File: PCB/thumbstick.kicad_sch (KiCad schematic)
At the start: 2 parts

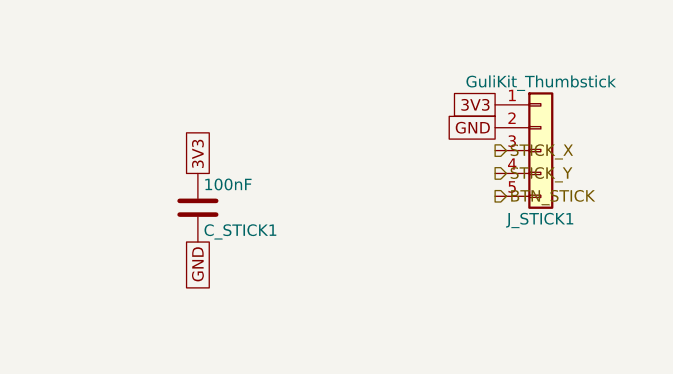
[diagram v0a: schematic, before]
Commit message: refactor: updated gulikit footprint
This updates the gulikit thumbstick footprint to be accurate.
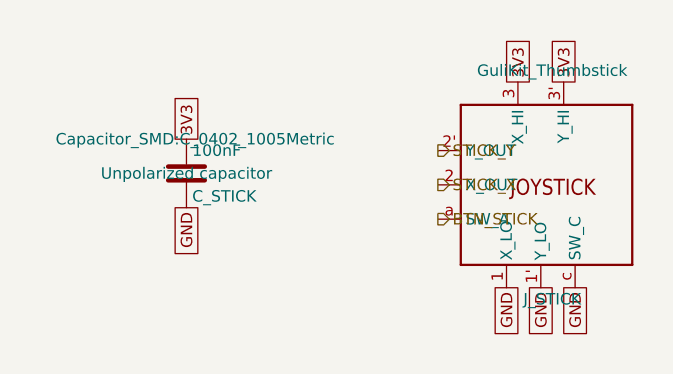
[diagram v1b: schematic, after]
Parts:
- removed C_STICK1: 100nF, Capacitor_SMD:C_0402_1005Metric, symbol Device:C
- removed J_STICK1: GuliKit_Thumbstick, Connector_PinHeader_2.54mm:PinHeader_1x05_P2.54mm_Vertical, symbol Connector_Generic:Conn_01x05
- added C_STICK: 100nF, Capacitor_SMD:C_0402_1005Metric, symbol Device:C
- added J_STICK: GuliKit_Thumbstick, SnipsControllers_Custom:GuliKit_HallStick, symbol SnipsControllers_Custom:GuliKit_HallStick
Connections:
- net 3V3: now also C_STICK.1, J_STICK.3 (X_HI), J_STICK.3' (Y_HI)
- net BTN_STICK: now also J_STICK.a (SW_A)
- net GND: now also C_STICK.2, J_STICK.1 (X_LO), J_STICK.1' (Y_LO), J_STICK.c (SW_C)
- net STICK_X: now also J_STICK.2 (X_OUT)
- net STICK_Y: now also J_STICK.2' (Y_OUT)
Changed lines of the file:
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@@
 	(global_label "GND"
 		(shape passive)
-		(at 129.54 111.76 270)
+		(at 163.83 116.84 270)
 		(fields_autoplaced yes)
 		(effects
@@
 		)
 		(property "Intersheetrefs" "${INTERSHEET_REFS}"
-			(at 129.54 111.76 0)
+			(at 163.83 116.84 0)
+			(hide yes)
+			(show_name no)
+			(do_not_autoplace no)
+			(effects
+				(font
+					(size 1.27 1.27)
+				)
+			)
+		)
+	)
+	(global_label "GND"
+		(shape passive)
+		(at 128.27 107.95 270)
+		(fields_autoplaced yes)
+		(effects
+			(font
+				(size 1.27 1.27)
+			)
+			(justify right)
+		)
+		(property "Intersheetrefs" "${INTERSHEET_REFS}"
+			(at 128.27 107.95 0)
 			(hide yes)
 			(show_name no)
@@
 	(global_label "3V3"
 		(shape passive)
-		(at 162.56 96.52 180)
+		(at 128.27 100.33 90)
+		(fields_autoplaced yes)
+		(effects
+			(font
+				(size 1.27 1.27)
+			)
+			(justify left)
+		)
+		(property "Intersheetrefs" "${INTERSHEET_REFS}"
+			(at 128.27 100.33 0)
+			(hide yes)
+			(show_name no)
+			(do_not_autoplace no)
+			(effects
+				(font
+					(size 1.27 1.27)
+				)
+			)
+		)
+	)
+	(global_label "3V3"
+		(shape passive)
+		(at 165.1 93.98 90)
+		(fields_autoplaced yes)
+		(effects
+			(font
+				(size 1.27 1.27)
+			)
+			(justify left)
+		)
+		(property "Intersheetrefs" "${INTERSHEET_REFS}"
+			(at 165.1 93.98 0)
+			(hide yes)
+			(show_name no)
+			(do_not_autoplace no)
+			(effects
+				(font
+					(size 1.27 1.27)
+				)
+			)
+		)
+	)
+	(global_label "3V3"
+		(shape passive)
+		(at 170.18 93.98 90)
+		(fields_autoplaced yes)
+		(effects
+			(font
+				(size 1.27 1.27)
+			)
+			(justify left)
+		)
+		(property "Intersheetrefs" "${INTERSHEET_REFS}"
+			(at 170.18 93.98 0)
+			(hide yes)
+			(show_name no)
+			(do_not_autoplace no)
+			(effects
+				(font
+					(size 1.27 1.27)
+				)
+			)
+		)
+	)
+	(global_label "GND"
+		(shape passive)
+		(at 171.45 116.84 270)
 		(fields_autoplaced yes)
 		(effects
@@
 		)
 		(property "Intersheetrefs" "${INTERSHEET_REFS}"
-			(at 162.56 96.52 0)
-			(hide yes)
-			(show_name no)
-			(do_not_autoplace no)
-			(effects
-				(font
-					(size 1.27 1.27)
-				)
-			)
-		)
-	)
-	(global_label "3V3"
-		(shape passive)
-		(at 129.54 104.14 90)
-		(fields_autoplaced yes)
-		(effects
-			(font
-				(size 1.27 1.27)
-			)
-			(justify left)
-		)
-		(property "Intersheetrefs" "${INTERSHEET_REFS}"
-			(at 129.54 104.14 0)
+			(at 171.45 116.84 0)
 			(hide yes)
 			(show_name no)
@@
 	(global_label "GND"
 		(shape passive)
-		(at 162.56 99.06 180)
+		(at 167.64 116.84 270)
 		(fields_autoplaced yes)
 		(effects
@@
 		)
 		(property "Intersheetrefs" "${INTERSHEET_REFS}"
-			(at 162.56 99.06 0)
-			(hide yes)
-			(show_name no)
-			(do_not_autoplace no)
-			(effects
-				(font
-					(size 1.27 1.27)
-				)
-			)
+			(at 167.64 116.84 0)
+			(hide yes)
+			(show_name no)
+			(do_not_autoplace no)
+			(effects
+				(font
+					(size 1.27 1.27)
+				)
+			)
+		)
+	)
+	(hierarchical_label "STICK_Y"
+		(shape output)
+		(at 156.21 101.6 0)
+		(effects
+			(font
+				(size 1.27 1.27)
+			)
+			(justify left)
+		)
+	)
+	(hierarchical_label "BTN_STICK"
+		(shape output)
+		(at 156.21 109.22 0)
+		(effects
+			(font
+				(size 1.27 1.27)
+			)
+			(justify left)
 		)
 	)
 	(hierarchical_label "STICK_X"
 		(shape output)
-		(at 162.56 101.6 0)
-		(effects
-			(font
-				(size 1.27 1.27)
-			)
-			(justify left)
-		)
-	)
-	(hierarchical_label "BTN_STICK"
-		(shape output)
-		(at 162.56 106.68 0)
-		(effects
-			(font
-				(size 1.27 1.27)
-			)
-			(justify left)
-		)
-	)
-	(hierarchical_label "STICK_Y"
-		(shape output)
-		(at 162.56 104.14 0)
+		(at 156.21 105.41 0)
 		(effects
 			(font
@@
 	)
 	(symbol
-		(lib_id "Connector_Generic:Conn_01x05")
-		(at 167.64 101.6 0)
+		(lib_id "Device:C")
+		(at 128.27 104.14 0)
 		(unit 1)
 		(body_style 1)
@@
 		(dnp no)
 		(fields_autoplaced yes)
-		(property "Reference" "J_STICK1"
-			(at 167.64 109.22 0)
-			(show_name no)
-			(do_not_autoplace no)
-			(effects
-				(font
-					(size 1.27 1.27)
-				)
-			)
-		)
-		(property "Value" "GuliKit_Thumbstick"
-			(at 167.64 93.98 0)
-			(show_name no)
-			(do_not_autoplace no)
-			(effects
-				(font
-					(size 1.27 1.27)
-				)
-			)
-		)
-		(property "Footprint" "Connector_PinHeader_2.54mm:PinHeader_1x05_P2.54mm_Vertical"
-			(at 167.64 101.6 0)
-			(hide yes)
+		(property "Reference" "C_STICK"
+			(at 128.905 106.68 0)
+			(show_name no)
+			(do_not_autoplace no)
+			(effects
+				(font
+					(size 1.27 1.27)
+				)
+				(justify left)
+			)
+		)
+		(property "Value" "100nF"
+			(at 128.905 101.6 0)
+			(show_name no)
+			(do_not_autoplace no)
+			(effects
+				(font
+					(size 1.27 1.27)
+				)
+				(justify left)
+			)
+		)
+		(property "Footprint" "Capacitor_SMD:C_0402_1005Metric"
+			(at 129.2352 100.33 0)
 			(show_name no)
 			(do_not_autoplace no)
@@
 		)
 		(property "Datasheet" ""
-			(at 167.64 101.6 0)
-			(hide yes)
-			(show_name no)
-			(do_not_autoplace no)
-			(effects
-				(font
-					(size 1.27 1.27)
-				)
-			)
-		)
-		(property "Description" "Generic connector, single row, 01x05, script generated (kicad-library-utils/schlib/autogen/connector/)"
-			(at 167.64 101.6 0)
-			(hide yes)
+			(at 128.27 104.14 0)
+			(show_name no)
+			(do_not_autoplace no)
+			(effects
+				(font
+					(size 1.27 1.27)
+				)
+			)
+		)
+		(property "Description" "Unpolarized capacitor"
+			(at 128.27 104.14 0)
 			(show_name no)
 			(do_not_autoplace no)
@@
 		(pin "2"
 		)
-		(pin "3"
-		)
-		(pin "4"
-		)
-		(pin "5"
-		)
 		(instances
-			(project "snips_controller"
-				(path "/868f8289-8434-4465-b2f4-2accc5e40bab/7a3e413b-2e94-4a8b-a1cc-2db3e975d99a"
-					(reference "J_STICK1")
+			(project ""
+				(path "/d0f5b7d7-b2b6-4492-958c-e60265d3c6b4/d3a109f9-ed10-4138-8f18-30dfb6d6156b"
+					(reference "C_STICK")
 					(unit 1)
 				)
@@
 	)
 	(symbol
-		(lib_id "Device:C")
-		(at 129.54 107.95 0)
+		(lib_id "SnipsControllers_Custom:GuliKit_HallStick")
+		(at 168.91 105.41 0)
 		(unit 1)
 		(body_style 1)
@@
 		(dnp no)
 		(fields_autoplaced yes)
-		(property "Reference" "C_STICK1"
-			(at 130.175 110.49 0)
-			(show_name no)
-			(do_not_autoplace no)
-			(effects
-				(font
-					(size 1.27 1.27)
-				)
-				(justify left)
-			)
-		)
-		(property "Value" "100nF"
-			(at 130.175 105.41 0)
-			(show_name no)
-			(do_not_autoplace no)
-			(effects
-				(font
-					(size 1.27 1.27)
-				)
-				(justify left)
-			)
-		)
-		(property "Footprint" "Capacitor_SMD:C_0402_1005Metric"
-			(at 130.5052 104.14 0)
+		(property "Reference" "J_STICK"
+			(at 168.91 118.11 0)
+			(show_name no)
+			(do_not_autoplace no)
+			(effects
+				(font
+					(size 1.27 1.27)
+				)
+			)
+		)
+		(property "Value" "GuliKit_Thumbstick"
+			(at 168.91 92.71 0)
+			(show_name no)
+			(do_not_autoplace no)
+			(effects
+				(font
+					(size 1.27 1.27)
+				)
+			)
+		)
+		(property "Footprint" "SnipsControllers_Custom:GuliKit_HallStick"
+			(at 168.91 105.41 0)
 			(hide yes)
 			(show_name no)
@@
 		)
 		(property "Datasheet" ""
-			(at 129.54 107.95 0)
-			(hide yes)
-			(show_name no)
-			(do_not_autoplace no)
-			(effects
-				(font
-					(size 1.27 1.27)
-				)
-			)
-		)
-		(property "Description" "Unpolarized capacitor"
-			(at 129.54 107.95 0)
+			(at 168.91 105.41 0)
+			(hide yes)
+			(show_name no)
+			(do_not_autoplace no)
+			(effects
+				(font
+					(size 1.27 1.27)
+				)
+			)
+		)
+		(property "Description" "OEM-replacement-style hall/TMR analog thumbstick with center-push switch (ALPS RKJXV1224 / C&K THB001P footprint family). 2-axis potentiometer-emulation interface, not a simple VCC/GND/X/Y/SW breakout: pins 1/2/3 are the X axis low/wiper/high, pins 1'/2'/3' are the Y axis low/wiper/high, pins a/c are the switch (b/d are mechanically-redundant duplicate switch legs, intentionally unconnected). Drive 1 and 1' to GND, 3 and 3' to 3V3; read wipers 2 (X) and 2' (Y) on ADC pins; wire switch a to a GPIO and c to GND. Adapted from dbenoy/thumbstick-breakout (CC-BY-SA 4.0, Copyright (c) Daniel Benoy)."
+			(at 168.91 105.41 0)
 			(hide yes)
 			(show_name no)
@@
 		(pin "1"
 		)
+		(pin "1'"
+		)
 		(pin "2"
 		)
+		(pin "2'"
+		)
+		(pin "3"
+		)
+		(pin "3'"
+		)
+		(pin "a"
+		)
+		(pin "c"
+		)
 		(instances
-			(project "snips_controller"
-				(path "/868f8289-8434-4465-b2f4-2accc5e40bab/7a3e413b-2e94-4a8b-a1cc-2db3e975d99a"
-					(reference "C_STICK1")
+			(project ""
+				(path "/d0f5b7d7-b2b6-4492-958c-e60265d3c6b4/d3a109f9-ed10-4138-8f18-30dfb6d6156b"
+					(reference "J_STICK")
 					(unit 1)
 				)

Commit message: layout: beginning pcb layout
This updates the schematic with a few different footprints while also starts the layout.
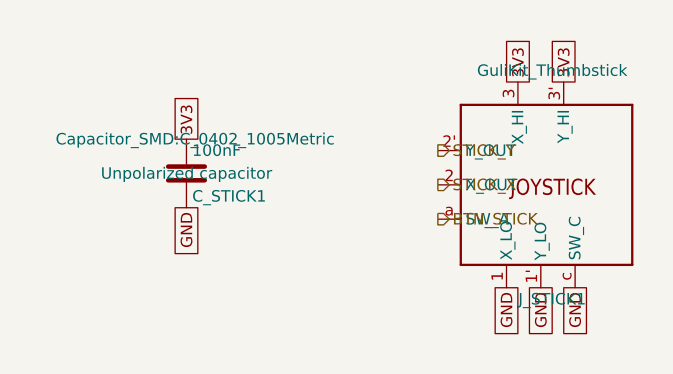
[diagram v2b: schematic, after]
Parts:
- renumbered C_STICK to C_STICK1, J_STICK to J_STICK1
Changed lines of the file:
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@@
 		(dnp no)
 		(fields_autoplaced yes)
-		(property "Reference" "C_STICK"
+		(property "Reference" "C_STICK1"
 			(at 128.905 106.68 0)
 			(show_name no)
@@
 		)
 		(instances
+			(project "snips_controller"
+				(path "/868f8289-8434-4465-b2f4-2accc5e40bab/d3a109f9-ed10-4138-8f18-30dfb6d6156b"
+					(reference "C_STICK1")
+					(unit 1)
+				)
+			)
 			(project ""
 				(path "/d0f5b7d7-b2b6-4492-958c-e60265d3c6b4/d3a109f9-ed10-4138-8f18-30dfb6d6156b"
@@
 		(dnp no)
 		(fields_autoplaced yes)
-		(property "Reference" "J_STICK"
+		(property "Reference" "J_STICK1"
 			(at 168.91 118.11 0)
 			(show_name no)
@@
 		)
 		(instances
+			(project "snips_controller"
+				(path "/868f8289-8434-4465-b2f4-2accc5e40bab/d3a109f9-ed10-4138-8f18-30dfb6d6156b"
+					(reference "J_STICK1")
+					(unit 1)
+				)
+			)
 			(project ""
 				(path "/d0f5b7d7-b2b6-4492-958c-e60265d3c6b4/d3a109f9-ed10-4138-8f18-30dfb6d6156b"

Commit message: refactor: swap footprints and add symmetry
This updates the footprints of a couple components to be smaller and closer to what we want. It also adds two buttons to ensure left and right side symmetry.
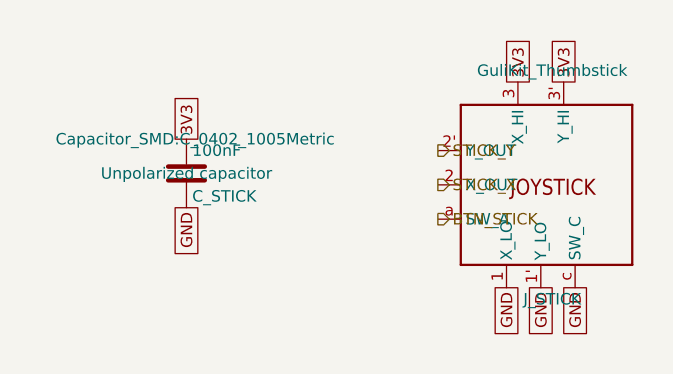
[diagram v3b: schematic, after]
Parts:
- removed C_STICK1: 100nF, Capacitor_SMD:C_0402_1005Metric, symbol Device:C
- removed J_STICK1: GuliKit_Thumbstick, SnipsControllers_Custom:GuliKit_HallStick, symbol SnipsControllers_Custom:GuliKit_HallStick
- added C_STICK: 100nF, Capacitor_SMD:C_0402_1005Metric, symbol Device:C
- added J_STICK: GuliKit_Thumbstick, SnipsControllers_Custom:GuliKit_HallStick, symbol SnipsControllers_Custom:GuliKit_HallStick
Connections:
- net 3V3: now also C_STICK.1, J_STICK.3 (X_HI), J_STICK.3' (Y_HI)
- net BTN_STICK: now also J_STICK.a (SW_A)
- net GND: now also C_STICK.2, J_STICK.1 (X_LO), J_STICK.1' (Y_LO), J_STICK.c (SW_C)
- net STICK_X: now also J_STICK.2 (X_OUT)
- net STICK_Y: now also J_STICK.2' (Y_OUT)
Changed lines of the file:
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@@
 	(global_label "GND"
 		(shape passive)
+		(at 167.64 116.84 270)
+		(fields_autoplaced yes)
+		(effects
+			(font
+				(size 1.27 1.27)
+			)
+			(justify right)
+		)
+		(property "Intersheetrefs" "${INTERSHEET_REFS}"
+			(at 167.64 116.84 0)
+			(hide yes)
+			(show_name no)
+			(do_not_autoplace no)
+			(effects
+				(font
+					(size 1.27 1.27)
+				)
+			)
+		)
+	)
+	(global_label "GND"
+		(shape passive)
+		(at 128.27 107.95 270)
+		(fields_autoplaced yes)
+		(effects
+			(font
+				(size 1.27 1.27)
+			)
+			(justify right)
+		)
+		(property "Intersheetrefs" "${INTERSHEET_REFS}"
+			(at 128.27 107.95 0)
+			(hide yes)
+			(show_name no)
+			(do_not_autoplace no)
+			(effects
+				(font
+					(size 1.27 1.27)
+				)
+			)
+		)
+	)
+	(global_label "3V3"
+		(shape passive)
+		(at 170.18 93.98 90)
+		(fields_autoplaced yes)
+		(effects
+			(font
+				(size 1.27 1.27)
+			)
+			(justify left)
+		)
+		(property "Intersheetrefs" "${INTERSHEET_REFS}"
+			(at 170.18 93.98 0)
+			(hide yes)
+			(show_name no)
+			(do_not_autoplace no)
+			(effects
+				(font
+					(size 1.27 1.27)
+				)
+			)
+		)
+	)
+	(global_label "3V3"
+		(shape passive)
+		(at 128.27 100.33 90)
+		(fields_autoplaced yes)
+		(effects
+			(font
+				(size 1.27 1.27)
+			)
+			(justify left)
+		)
+		(property "Intersheetrefs" "${INTERSHEET_REFS}"
+			(at 128.27 100.33 0)
+			(hide yes)
+			(show_name no)
+			(do_not_autoplace no)
+			(effects
+				(font
+					(size 1.27 1.27)
+				)
+			)
+		)
+	)
+	(global_label "GND"
+		(shape passive)
+		(at 171.45 116.84 270)
+		(fields_autoplaced yes)
+		(effects
+			(font
+				(size 1.27 1.27)
+			)
+			(justify right)
+		)
+		(property "Intersheetrefs" "${INTERSHEET_REFS}"
+			(at 171.45 116.84 0)
+			(hide yes)
+			(show_name no)
+			(do_not_autoplace no)
+			(effects
+				(font
+					(size 1.27 1.27)
+				)
+			)
+		)
+	)
+	(global_label "GND"
+		(shape passive)
 		(at 163.83 116.84 270)
 		(fields_autoplaced yes)
@@
 		)
 	)
-	(global_label "GND"
-		(shape passive)
-		(at 128.27 107.95 270)
-		(fields_autoplaced yes)
-		(effects
-			(font
-				(size 1.27 1.27)
-			)
-			(justify right)
-		)
-		(property "Intersheetrefs" "${INTERSHEET_REFS}"
-			(at 128.27 107.95 0)
-			(hide yes)
-			(show_name no)
-			(do_not_autoplace no)
-			(effects
-				(font
-					(size 1.27 1.27)
-				)
-			)
-		)
-	)
 	(global_label "3V3"
 		(shape passive)
-		(at 128.27 100.33 90)
-		(fields_autoplaced yes)
-		(effects
-			(font
-				(size 1.27 1.27)
-			)
-			(justify left)
-		)
-		(property "Intersheetrefs" "${INTERSHEET_REFS}"
-			(at 128.27 100.33 0)
-			(hide yes)
-			(show_name no)
-			(do_not_autoplace no)
-			(effects
-				(font
-					(size 1.27 1.27)
-				)
-			)
-		)
-	)
-	(global_label "3V3"
-		(shape passive)
 		(at 165.1 93.98 90)
 		(fields_autoplaced yes)
@@
 		)
 	)
-	(global_label "3V3"
-		(shape passive)
-		(at 170.18 93.98 90)
-		(fields_autoplaced yes)
-		(effects
-			(font
-				(size 1.27 1.27)
-			)
-			(justify left)
-		)
-		(property "Intersheetrefs" "${INTERSHEET_REFS}"
-			(at 170.18 93.98 0)
-			(hide yes)
-			(show_name no)
-			(do_not_autoplace no)
-			(effects
-				(font
-					(size 1.27 1.27)
-				)
-			)
-		)
-	)
-	(global_label "GND"
-		(shape passive)
-		(at 171.45 116.84 270)
-		(fields_autoplaced yes)
-		(effects
-			(font
-				(size 1.27 1.27)
-			)
-			(justify right)
-		)
-		(property "Intersheetrefs" "${INTERSHEET_REFS}"
-			(at 171.45 116.84 0)
-			(hide yes)
-			(show_name no)
-			(do_not_autoplace no)
-			(effects
-				(font
-					(size 1.27 1.27)
-				)
-			)
-		)
-	)
-	(global_label "GND"
-		(shape passive)
-		(at 167.64 116.84 270)
-		(fields_autoplaced yes)
-		(effects
-			(font
-				(size 1.27 1.27)
-			)
-			(justify right)
-		)
-		(property "Intersheetrefs" "${INTERSHEET_REFS}"
-			(at 167.64 116.84 0)
-			(hide yes)
-			(show_name no)
-			(do_not_autoplace no)
-			(effects
-				(font
-					(size 1.27 1.27)
-				)
-			)
+	(hierarchical_label "STICK_X"
+		(shape output)
+		(at 156.21 105.41 0)
+		(effects
+			(font
+				(size 1.27 1.27)
+			)
+			(justify left)
+		)
+	)
+	(hierarchical_label "BTN_STICK"
+		(shape output)
+		(at 156.21 109.22 0)
+		(effects
+			(font
+				(size 1.27 1.27)
+			)
+			(justify left)
 		)
 	)
@@
 		(shape output)
 		(at 156.21 101.6 0)
-		(effects
-			(font
-				(size 1.27 1.27)
-			)
-			(justify left)
-		)
-	)
-	(hierarchical_label "BTN_STICK"
-		(shape output)
-		(at 156.21 109.22 0)
-		(effects
-			(font
-				(size 1.27 1.27)
-			)
-			(justify left)
-		)
-	)
-	(hierarchical_label "STICK_X"
-		(shape output)
-		(at 156.21 105.41 0)
 		(effects
 			(font
@@
 		(dnp no)
 		(fields_autoplaced yes)
-		(property "Reference" "C_STICK1"
+		(property "Reference" "C_STICK"
 			(at 128.905 106.68 0)
 			(show_name no)
@@
 		(instances
 			(project "snips_controller"
-				(path "/868f8289-8434-4465-b2f4-2accc5e40bab/d3a109f9-ed10-4138-8f18-30dfb6d6156b"
-					(reference "C_STICK1")
-					(unit 1)
-				)
-			)
-			(project ""
-				(path "/d0f5b7d7-b2b6-4492-958c-e60265d3c6b4/d3a109f9-ed10-4138-8f18-30dfb6d6156b"
+				(path "/f9d779c6-e1a6-4677-9004-6e9cc3d2fa8d/0d5246ec-5d9d-43ad-8a08-fe1da78eed54"
 					(reference "C_STICK")
 					(unit 1)
@@
 		(dnp no)
 		(fields_autoplaced yes)
-		(property "Reference" "J_STICK1"
+		(property "Reference" "J_STICK"
 			(at 168.91 118.11 0)
 			(show_name no)
@@
 		(instances
 			(project "snips_controller"
-				(path "/868f8289-8434-4465-b2f4-2accc5e40bab/d3a109f9-ed10-4138-8f18-30dfb6d6156b"
-					(reference "J_STICK1")
-					(unit 1)
-				)
-			)
-			(project ""
-				(path "/d0f5b7d7-b2b6-4492-958c-e60265d3c6b4/d3a109f9-ed10-4138-8f18-30dfb6d6156b"
+				(path "/f9d779c6-e1a6-4677-9004-6e9cc3d2fa8d/0d5246ec-5d9d-43ad-8a08-fe1da78eed54"
 					(reference "J_STICK")
 					(unit 1)
